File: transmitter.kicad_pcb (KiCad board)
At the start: 6 copper layers, 100 x 100 mm, 250 parts, among them IC1 W9864G6KH-6, IC2 TPS61165DBVR, IC3 MT25QL128ABA1ESE-0SIT, IC4 USBLC6-2SC6, J1 AFC07-S40ECA-00, J11 AFC07-S10FCC-00, J3 B2B-PH-K-S, J4 B2B-PH-K-S, J5 B3B-PH-K-S, J6 USB4085-GF-A, J7 Conn_01x05, J9 Conn_02x06_Odd_Even, Q1 AO3400A, Q2 AO3400A, Q3 SI2301CDS-T1-GE3, Q4 AO3400A, SW1 Button SPST SMD Tactile Switch, SW2 Button SPST SMD Tactile Switch, SW3 Button SPST SMD Tactile Switch, SW4 Button SPST SMD Tactile Switch, SW5 Button SPST SMD Tactile Switch, SW6 Button SPST SMD Tactile Switch, SW7 SW_SPDT_MSM, SW8 Button SPST SMD Tactile Switch, SW9 RotaryEncoder_Switch, U1 STM32H743ZIT6TR, U2 CAT24C256, U3 MP2667GG-0000-Z, U4 AMS1117-3.3, U5 TPS61252DSG, U6 PCA9554APW, Y1 32.768KHZ, Y2 X322525MOB4SI-25MHz

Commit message: routing backlight converter
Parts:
- moved C34 85.8 mm to (51.1, 52.0)
- moved R34 85.8 mm to (56.2, 49.4)
- moved R35 85.8 mm to (56.2, 51.4)
- moved S2 85.8 mm to (52.5, 44.3)
- moved C27 73.4 mm to (53.1, 64.8)
- moved C30 73.4 mm to (57.8, 64.8)
- moved C32 73.4 mm to (47.7, 64.7)
- moved R20 73.4 mm to (51.2, 64.8)
- moved R21 73.4 mm to (52.6, 63.3)
- moved R26 73.4 mm to (57.3, 63.3)
- moved R27 73.4 mm to (55.9, 64.8)
- moved R30 73.4 mm to (47.2, 63.2)
- moved R31 73.4 mm to (45.8, 64.7)
- moved SW1 73.4 mm to (52.6, 68.4)
- moved SW4 73.4 mm to (57.3, 68.4)
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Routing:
- net /Project Architecture/LCD - Backlight/LCD_BACKLIGHT_V+: track 7.03 -> 0.00 mm
- net /Project Architecture/LCD - Backlight/LCD_BACKLIGHT_V-: track 3.56 -> 0.00 mm, vias 0 -> 9
- net /Project Architecture/Auxiliary/NRST: track 0.00 -> 1.14 mm, vias 0 -> 1
- net VSYS_SW: vias 7 -> 11
- added copper zone on F.Cu, net /Project Architecture/LCD - Backlight/BLHV
- added copper zone on F.Cu, net /Project Architecture/LCD - Backlight/LCD_BACKLIGHT_V+
- added copper zone on F.Cu, net /Project Architecture/LCD - Backlight/LCD_BACKLIGHT_V-
- added copper zone on In2.Cu, net /Project Architecture/LCD - Backlight/LCD_BACKLIGHT_V-
- added copper zone on In2.Cu, net VSYS_SW

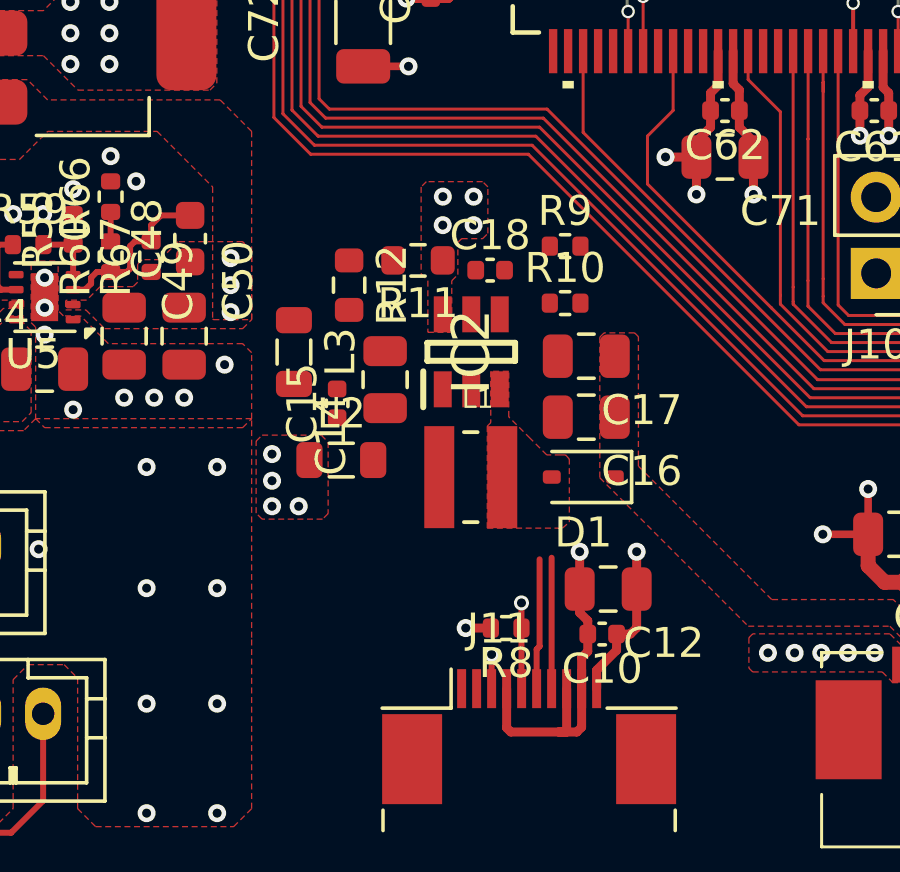
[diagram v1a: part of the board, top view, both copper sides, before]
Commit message: backlight converter routed
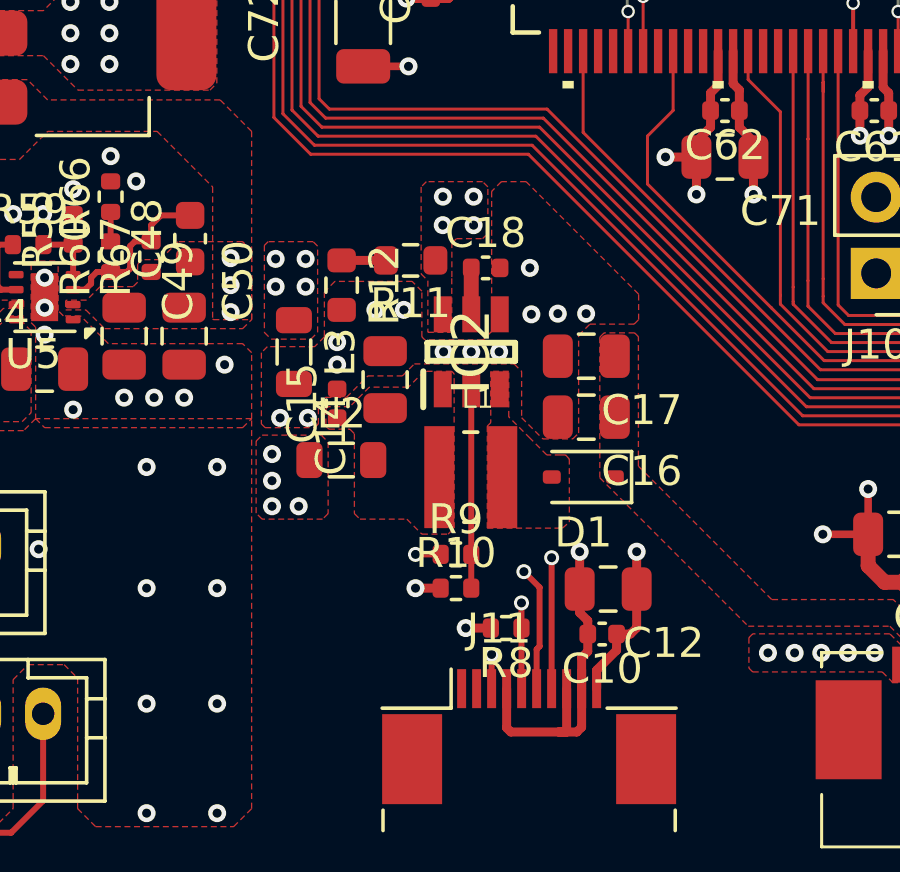
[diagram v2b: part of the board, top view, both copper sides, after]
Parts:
- moved R9 10.9 mm to (105.5, 110.8)
- moved R10 10.2 mm to (105.5, 111.9)
- moved R12 0.25 mm to (101.7, 101.8)
- moved R11 0.25 mm to (104.0, 101.0)
- moved C18 0.17 mm to (106.5, 101.2)
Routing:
- net /Project Architecture/LCD - Backlight/CTRL: track 0.00 -> 6.63 mm
- net Net-(IC2-COMP): track 0.00 -> 1.55 mm
- net Net-(R11-Pad2): track 0.00 -> 1.47 mm
- net GND: track 109.0 -> 109.8 mm, vias 128 -> 133
- net /Project Architecture/LCD - Backlight/BACKLIGHT_PWM: track 1.87 -> 2.71 mm, vias 1 -> 2
- net /Project Architecture/LCD - Connectors/I2C3_SDA: track 4.35 -> 4.16 mm, vias 0 -> 1
- net BLGND: vias 0 -> 13
- net /Project Architecture/LCD - Connectors/I2C3_SCL: vias 0 -> 1
- added copper zone on F.Cu, net BLGND
- added copper zone on In1.Cu, net BLGND
- added copper zone on F.Cu, net BLVDD

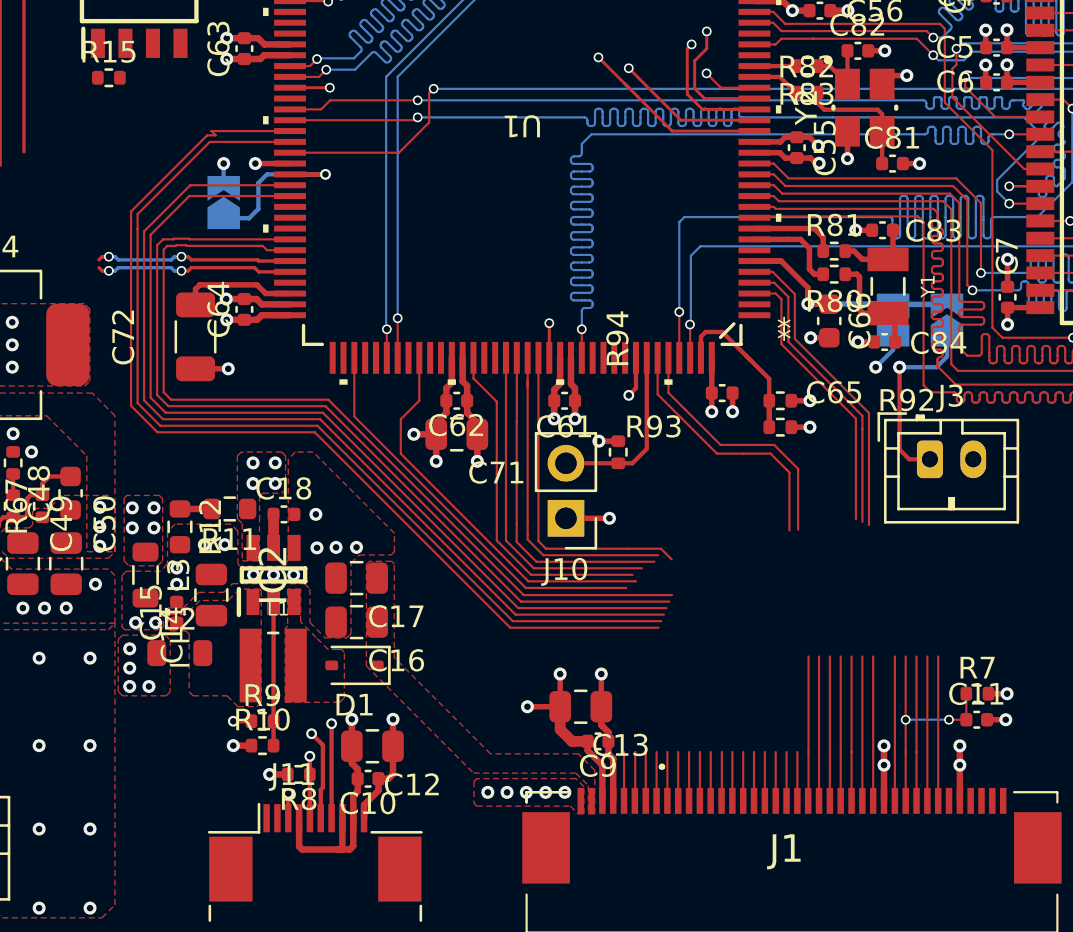
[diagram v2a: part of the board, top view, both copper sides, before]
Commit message: lcd connector routing
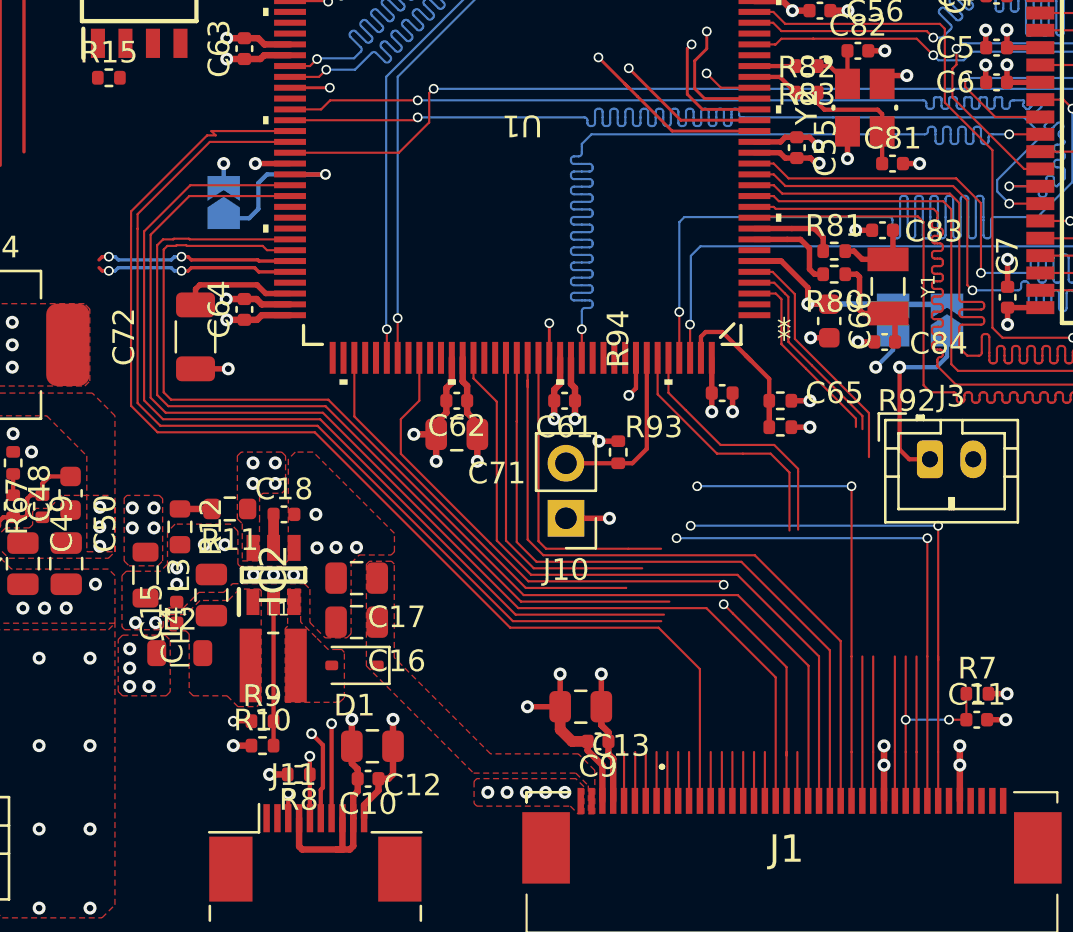
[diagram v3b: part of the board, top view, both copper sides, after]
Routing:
- net /Project Architecture/LCD - Connectors/LTDC_DE: track 27.8 -> 48.8 mm, vias 1 -> 3
- net /Project Architecture/LCD - Connectors/LTDC_VSYNC: track 34.3 -> 54.4 mm, vias 1 -> 3
- net /Project Architecture/LCD - Connectors/LTDC_B5: track 34.0 -> 49.6 mm, vias 1 -> 3
- net /Project Architecture/LCD - Connectors/LTDC_G7: track 20.3 -> 33.5 mm, vias 0 -> 2
- net /Project Architecture/LCD - Connectors/LTDC_B4: track 21.7 -> 32.5 mm
- net /Project Architecture/LCD - Connectors/LTDC_B2: track 22.5 -> 32.6 mm
- net /Project Architecture/LCD - Connectors/LTDC_B3: track 21.9 -> 32.0 mm
- net /Project Architecture/LCD - Connectors/LTDC_G6: track 44.8 -> 54.6 mm
- net /Project Architecture/LCD - Connectors/LTDC_R1: track 28.6 -> 38.4 mm
- net /Project Architecture/LCD - Connectors/LTDC_R6: track 30.0 -> 38.2 mm
- net /Project Architecture/LCD - Connectors/LTDC_R3: track 29.9 -> 37.6 mm
- net /Project Architecture/LCD - Connectors/LTDC_G2: track 29.3 -> 36.9 mm
- net /Project Architecture/LCD - Connectors/LTDC_R4: track 29.1 -> 36.8 mm
- net /Project Architecture/LCD - Connectors/LTDC_B1: track 46.7 -> 53.9 mm
- net /Project Architecture/LCD - Connectors/LTDC_R7: track 49.1 -> 55.6 mm
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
